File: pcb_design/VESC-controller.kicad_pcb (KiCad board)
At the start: 4 copper layers, 160 x 90 mm, 341 parts, among them J1 GATE_DRIVER_CONN_U, J2 GATE_DRIVER_CONN_V, J3 GATE_DRIVER_CONN_W, J4 micro USB, J5 ACCEL, J6 REGEN, J7 12V, J8 V_BUS, J9 SWD, P1 HALL/Encoder, P101 CANBUS, P2 Resolver, P3 PWR_COMM, Q1 BSC340N08, Q2 2N7002PW, Q3 AO4805, Q4 SI2302, Q5 SI2302, SW1 BOOTLOADER, U1 STM32F40X_LQFP64, U10 LM2903DT, U11 LM3488, U12 OPA2376AIDR, U13 LM1117IMP-v.v, U14 OPA2376AIDR, U15 AD2S1205, U16 OPA2376AIDR, U17 LM2903DT, U18 SN74LVC1G, U19 AD8397, U2 ISO1050, U20 APX809, U21 NCV78Mxx, U3 OPA2376AIDR, U4 LM2903DT, U5 7400-TSSOP, U6 SN74ACT08PWR, U7 SN74ACT08PWR, U8 SN74AUP1G74, U9 LM22676QTJ-5.0, X1 ABM3B - 8MHz, X2 ABM3B - 8MHz

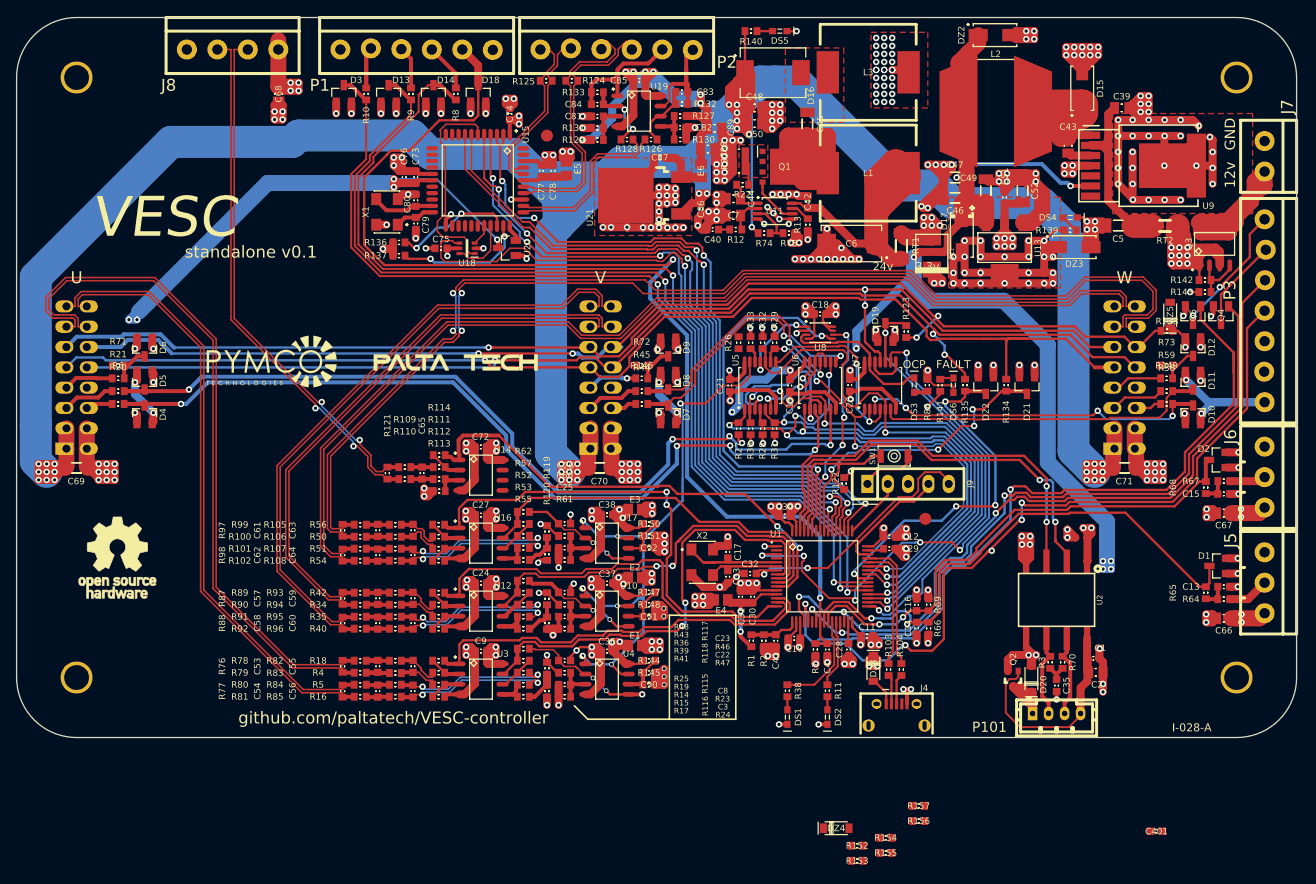
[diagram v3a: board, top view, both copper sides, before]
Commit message: Updated layout. DRC OK, moved silkscreen, bumped version to 0.2. Added portable 3d models
Signed-off-by: Marcos Chaparro <mchaparro@paltatech.com>
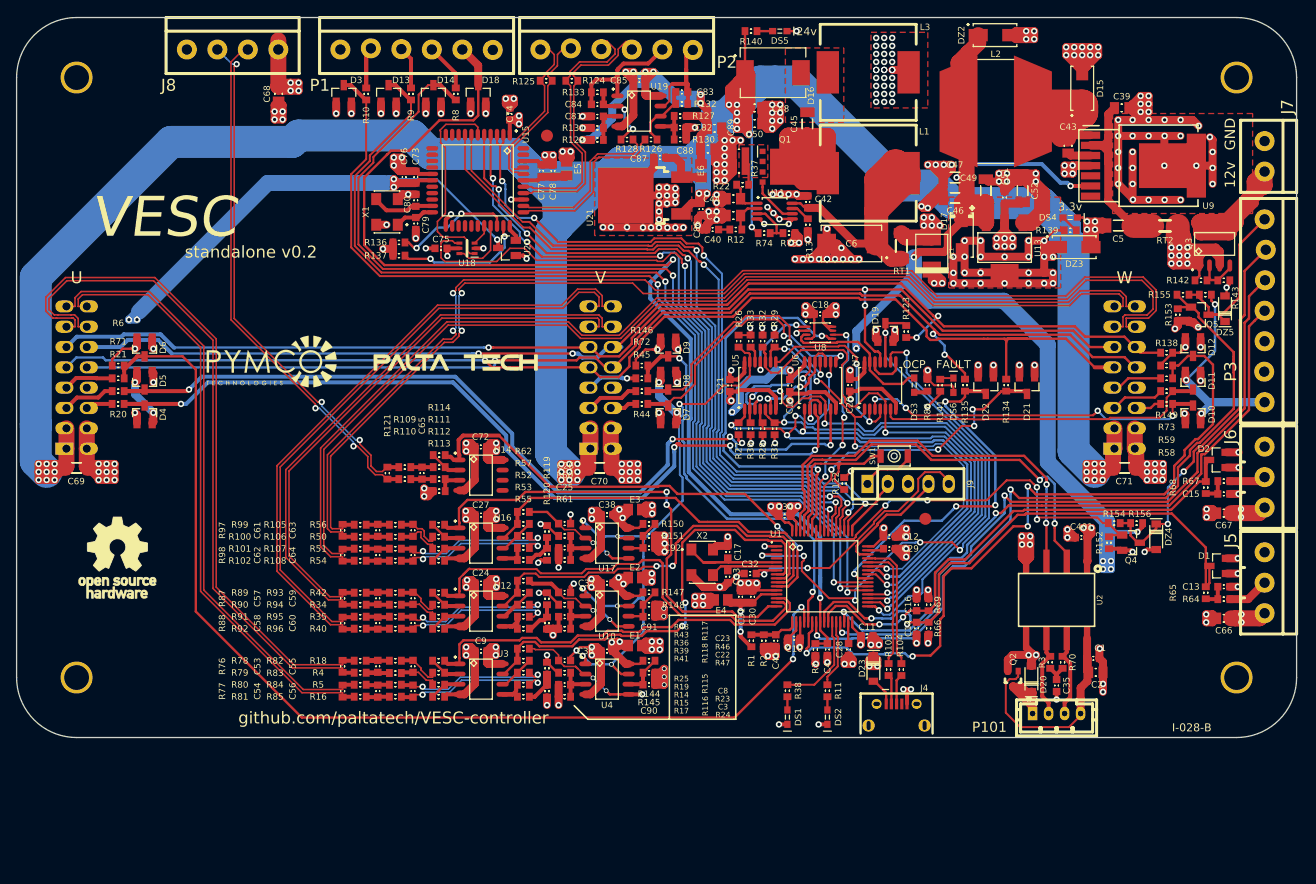
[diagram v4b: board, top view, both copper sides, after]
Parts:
- moved R153 79.2 mm to (65.2, -7.85), turned to 90 degrees
- moved R155 79.1 mm to (65.8, -10.3)
- moved R157 73.3 mm to (68.6, -10.3)
- moved DZ4 54.1 mm to (62.5, 19.9), turned to 270 degrees
- moved R152 49.3 mm to (56.5, 20.6), turned to 90 degrees
- moved R154 48.6 mm to (57.2, 18.2)
- moved R156 46.1 mm to (60.0, 18.2)
- moved C401 37.9 mm to (53.1, 20.0), turned to 180 degrees
- moved Q4 30.6 mm to (59.3, 20.6), turned to 0 degrees
- moved DZ5 6.90 mm to (71.0, -8.60)
- moved R143 2.77 mm to (70.9, -12.2), turned to 180 degrees
- moved R138 2.73 mm to (63.8, -3.10)
- moved Q5 0.85 mm to (67.9, -7.85), turned to 0 degrees
- moved R142 0.50 mm to (68.0, -12.2)
- moved R26 0.20 mm to (10.2, -4.55)
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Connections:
- J1 pad 13: /conditioning U/V_phase+ -> /conditioning U/V_phase-
- J1 pad 14: /conditioning U/V_phase- -> /conditioning U/V_phase+
- J1 pad 15: /conditioning U/I_phase+ -> /conditioning U/I_phase-
- J1 pad 16: /conditioning U/I_phase- -> /conditioning U/I_phase+
- J2 pad 13: /conditioning V/V_phase+ -> /conditioning V/V_phase-
- J2 pad 14: /conditioning V/V_phase- -> /conditioning V/V_phase+
- J2 pad 15: /conditioning V/I_phase+ -> /conditioning V/I_phase-
- J2 pad 16: /conditioning V/I_phase- -> /conditioning V/I_phase+
- J3 pad 13: /conditioning W/V_phase+ -> /conditioning W/V_phase-
- J3 pad 14: /conditioning W/V_phase- -> /conditioning W/V_phase+
- J3 pad 15: /conditioning W/I_phase+ -> /conditioning W/I_phase-
- J3 pad 16: /conditioning W/I_phase- -> /conditioning W/I_phase+
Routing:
- net /conditioning U/TEMP: track 4.34 -> 133.8 mm, vias 0 -> 2
- net /STM32F4/SCK_ADC_EXT: track 98.2 -> 0.00 mm, vias 5 -> 0
- net /conditioning W/TEMP: track 4.27 -> 93.3 mm, vias 0 -> 4
- net /Protected GPIOs/IN1: track 0.00 -> 49.6 mm, vias 0 -> 4
- net /conditioning V/TEMP: track 4.34 -> 51.3 mm, vias 0 -> 2
- net /Protected GPIOs/OUT1: track 11.6 -> 48.7 mm, vias 0 -> 2
- net +5: track 636.7 -> 654.7 mm, vias 36 -> 38
- net /STM32F4/RX_SDA_NSS: track 95.4 -> 82.0 mm, vias 3 -> 2
- net +3.3: track 179.6 -> 192.0 mm
- net GND: track 745.6 -> 754.6 mm, vias 325 -> 327
- net /Protected GPIOs/IN2: track 87.4 -> 94.9 mm, vias 1 -> 2
- net /Protected GPIOs/OUT2: track 16.8 -> 22.5 mm, vias 2 -> 0
- net /conditioning U/~OC_Fault: track 83.3 -> 86.5 mm
- net /STM32F4/ADC_15: track 68.3 -> 70.8 mm
- net /conditioning V/I_phase-: track 78.7 -> 76.7 mm
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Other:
- board text added: "I-028-B"
- board text added: "standalone v0.2"
- board text removed: "I-028-A"
- board text removed: "standalone v0.1"

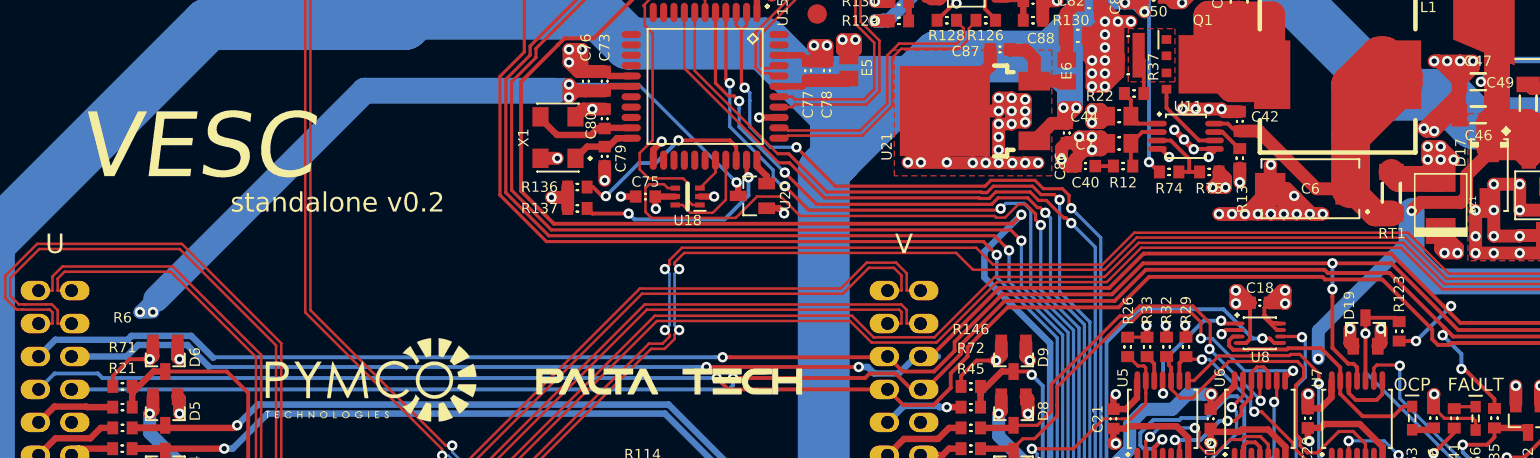
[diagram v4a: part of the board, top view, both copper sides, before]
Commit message: Added RC filter to FAULT line to prevent noise triggering it
Signed-off-by: Marcos Chaparro <mchaparro@paltatech.com>
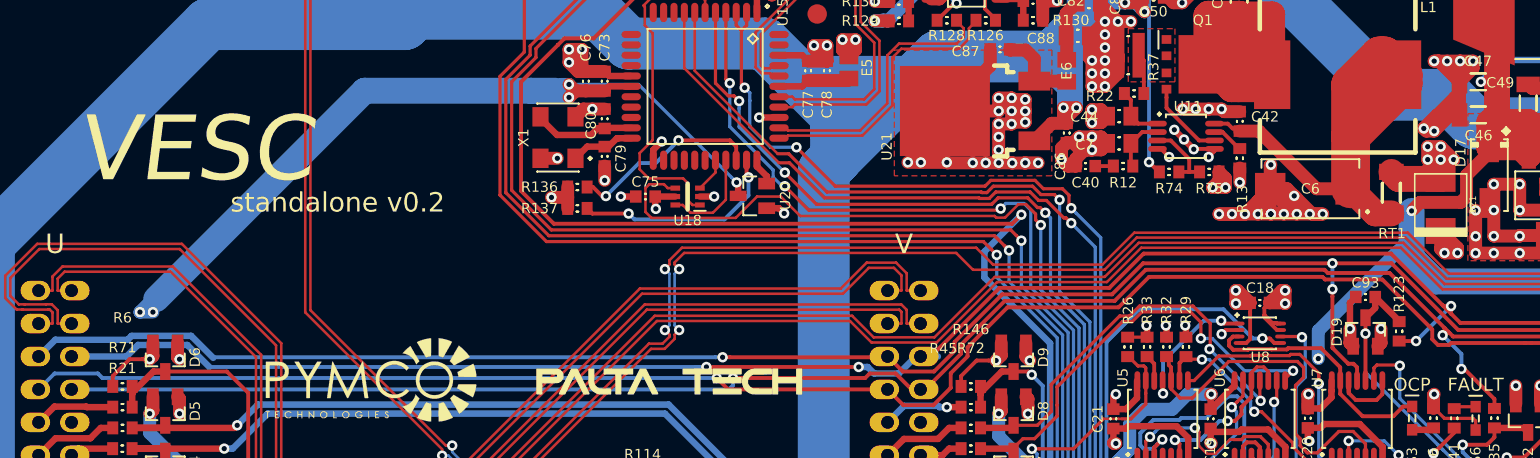
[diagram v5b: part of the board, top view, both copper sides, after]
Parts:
- added C93: 220pF, IPC7351-Nominal:CAPC1608X55, F.Cu at (28.6, -8.40)
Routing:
- net +5: track 654.7 -> 657.9 mm
- net GND: track 754.6 -> 757.3 mm
- net /STM32F4/~FAULT: track 61.4 -> 63.7 mm
- net ~FAULT: track 151.2 -> 152.4 mm
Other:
- board text removed: "PWR_GOOD"
